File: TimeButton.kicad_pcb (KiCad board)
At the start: 2 copper layers, 45.7 x 28.2 mm, 32 parts, among them J1 TagConnect, J3 USB_C_Receptacle_USB2.0_16P, U1 STM32F042G4Ux, U2 NCP1117ST33T3G, U3 M24C02-FMN

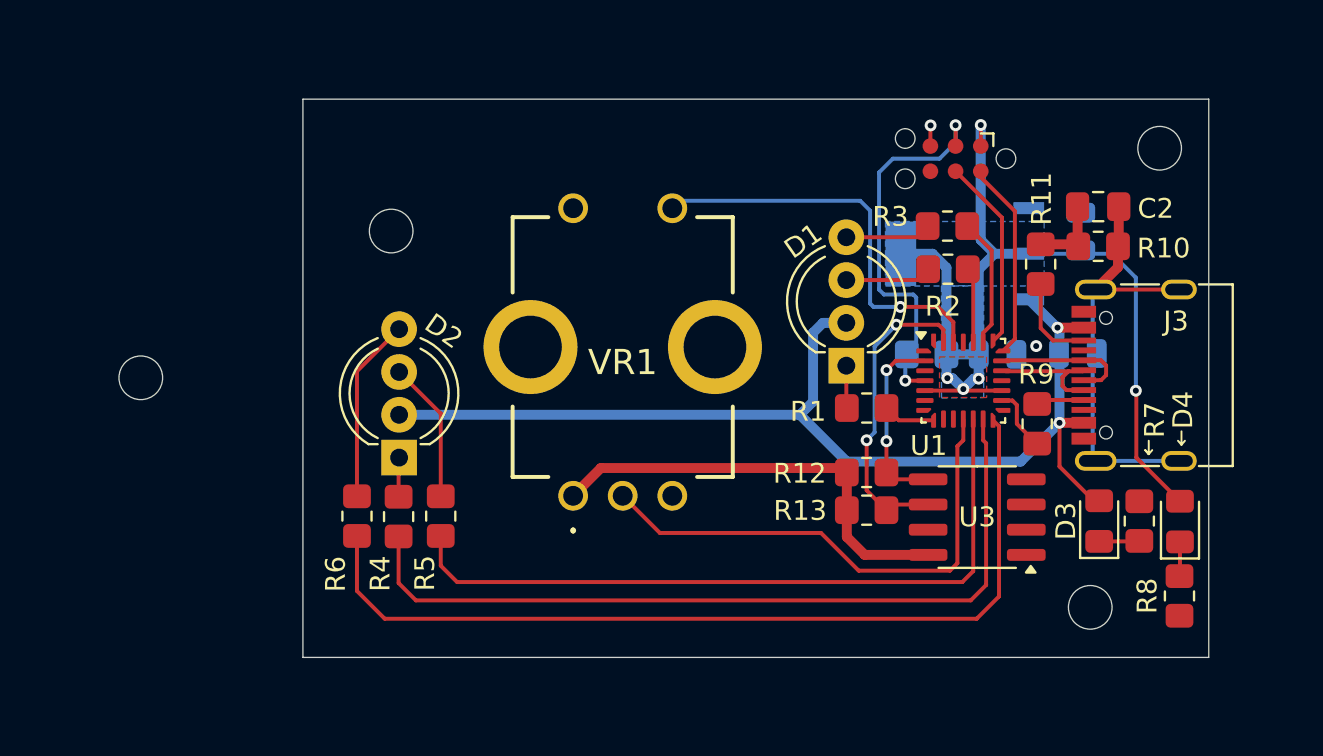
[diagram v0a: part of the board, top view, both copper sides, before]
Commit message: Added two GPIO Connectors for additional use
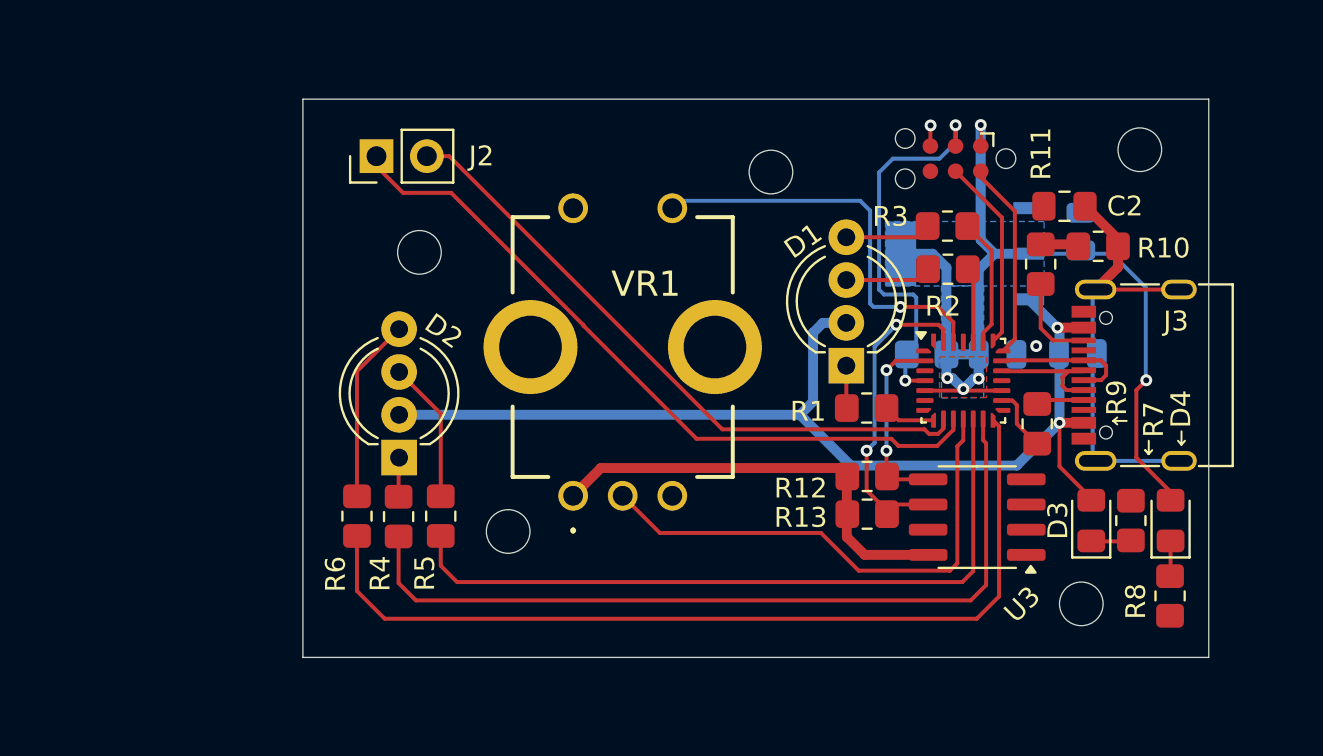
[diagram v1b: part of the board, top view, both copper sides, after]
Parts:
- added H5: MountingHole, MountingHole:MountingHole_2.2mm_M2_DIN965, F.Cu at (152.4, 89.2)
- added J2: Conn_01x02_Pin, Connector_PinHeader_2.54mm:PinHeader_1x02_P2.54mm_Vertical, F.Cu at (132.5, 88.4)
- moved H3 20.1 mm to (139.2, 107.3)
- moved H4 1.79 mm to (134.7, 93.2)
- moved C2 1.70 mm to (167.2, 90.9)
- moved H1 1.00 mm to (171.0, 88.0)
- moved H2 0.48 mm to (168.1, 111.0)
- moved D4 0.48 mm to (172.6, 106.8)
- moved R8 0.47 mm to (172.6, 110.5)
- moved R7 0.43 mm to (170.6, 106.8)
- moved D3 0.40 mm to (168.6, 106.8)
- moved R12 0.20 mm to (157.3, 104.5)
- moved R13 0.20 mm to (157.3, 106.4)
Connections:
- U1 pad 10: unconnected-(U1-PA4-Pad10) -> PA4
- U1 pad 9: unconnected-(U1-PA3-Pad9) -> PA3
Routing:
- net PA4: track 0.00 -> 36.3 mm
- net PA3: track 0.00 -> 32.4 mm
- net GND: track 8.17 -> 6.21 mm
- net Net-(J3-SHIELD): track 21.8 -> 22.5 mm

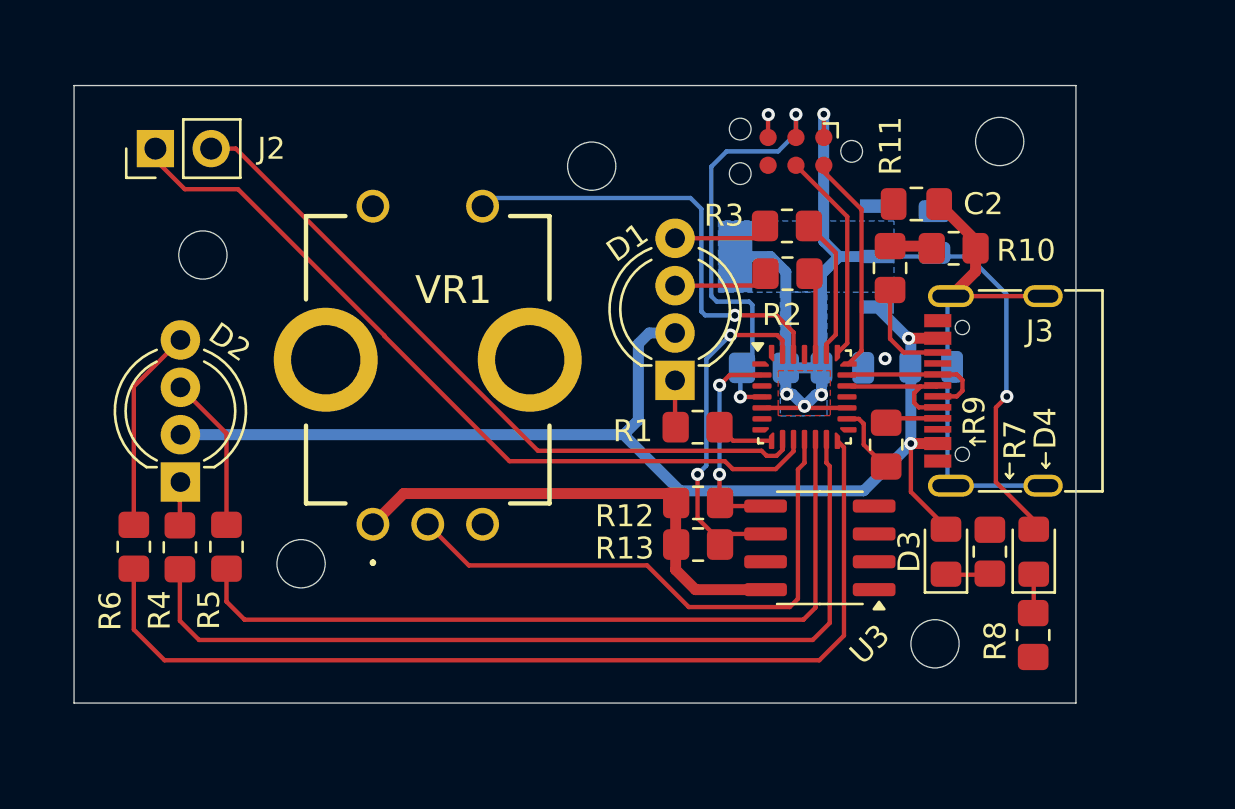
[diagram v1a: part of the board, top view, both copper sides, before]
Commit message: Added Capacitor for EEPROM
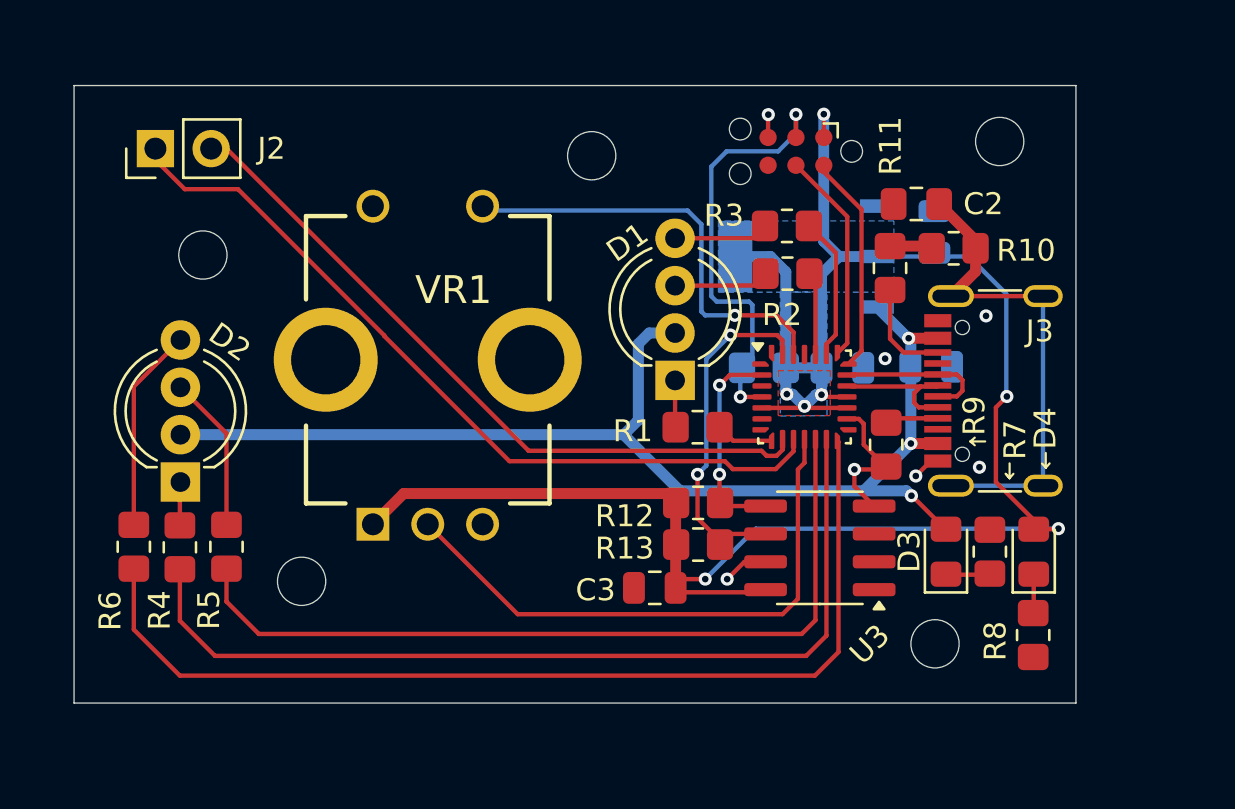
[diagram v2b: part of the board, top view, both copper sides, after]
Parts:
- added C3: 22pF, Capacitor_SMD:C_0805_2012Metric, F.Cu at (155.3, 108.4)
- moved H3 0.80 mm to (139.2, 108.1)
- moved H5 0.47 mm to (152.4, 88.7)
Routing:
- net 3.3V: track 72.8 -> 94.3 mm, vias 5 -> 7
- net GND: track 6.21 -> 13.1 mm, vias 2 -> 7
- net PWM3_G: track 36.6 -> 37.5 mm
- net PWM3_R: track 41.1 -> 41.8 mm
- net nButton: track 20.6 -> 19.9 mm
- net PWM3_B: track 45.2 -> 45.9 mm
- net 5V: track 55.6 -> 55.7 mm, vias 2 -> 3
